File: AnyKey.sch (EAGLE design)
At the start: 101 parts, among them SW1 EVQQ, SW10 EVQQ, SW2 EVQQ, SW3 EVQQ, SW4 EVQQ, SW5 EVQQ, SW6 EVQQ, SW7 EVQQ, SW8 EVQQ, SW9 EVQQ, U3 AP2112K-3.3V

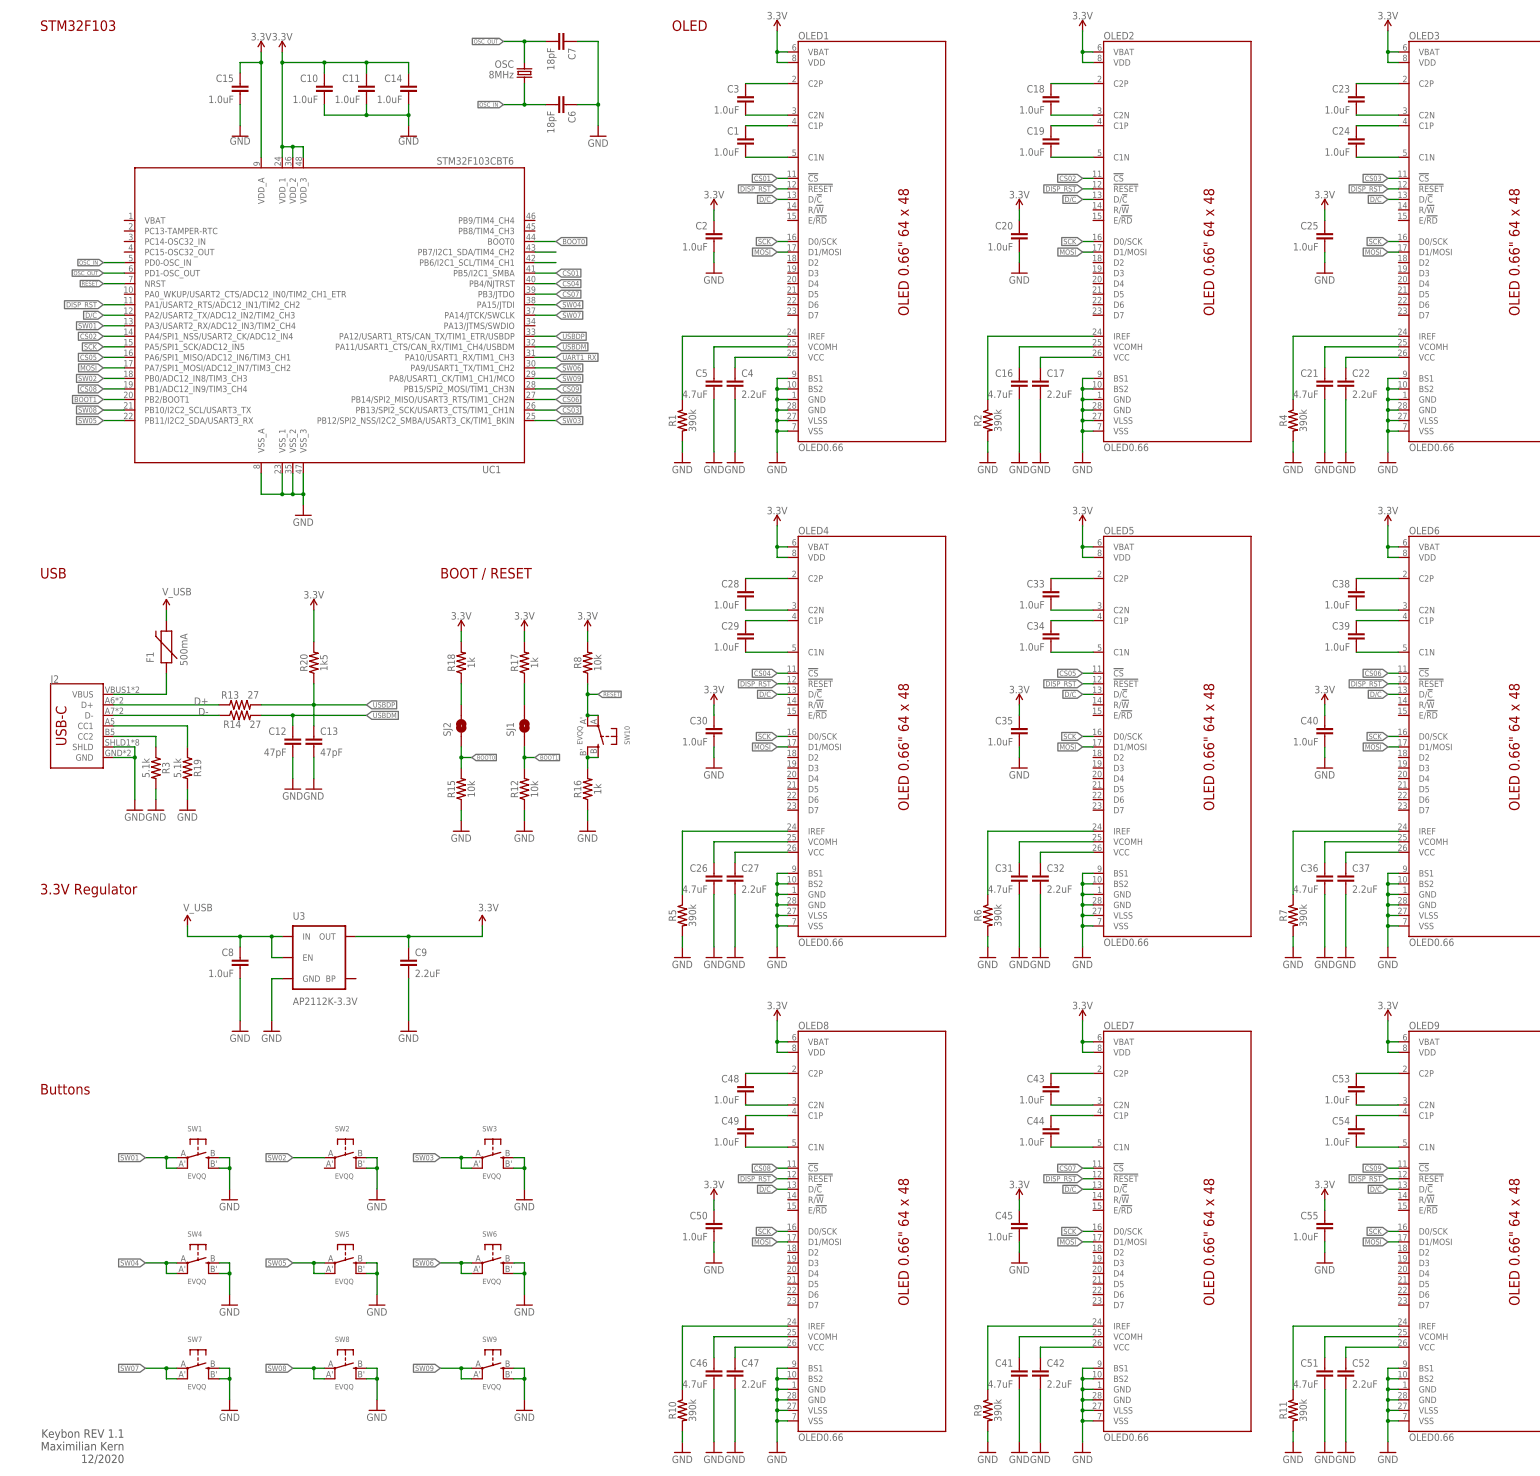
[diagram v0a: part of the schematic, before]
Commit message: Initial cleanup, correctted some misplaced names in top silkscreen
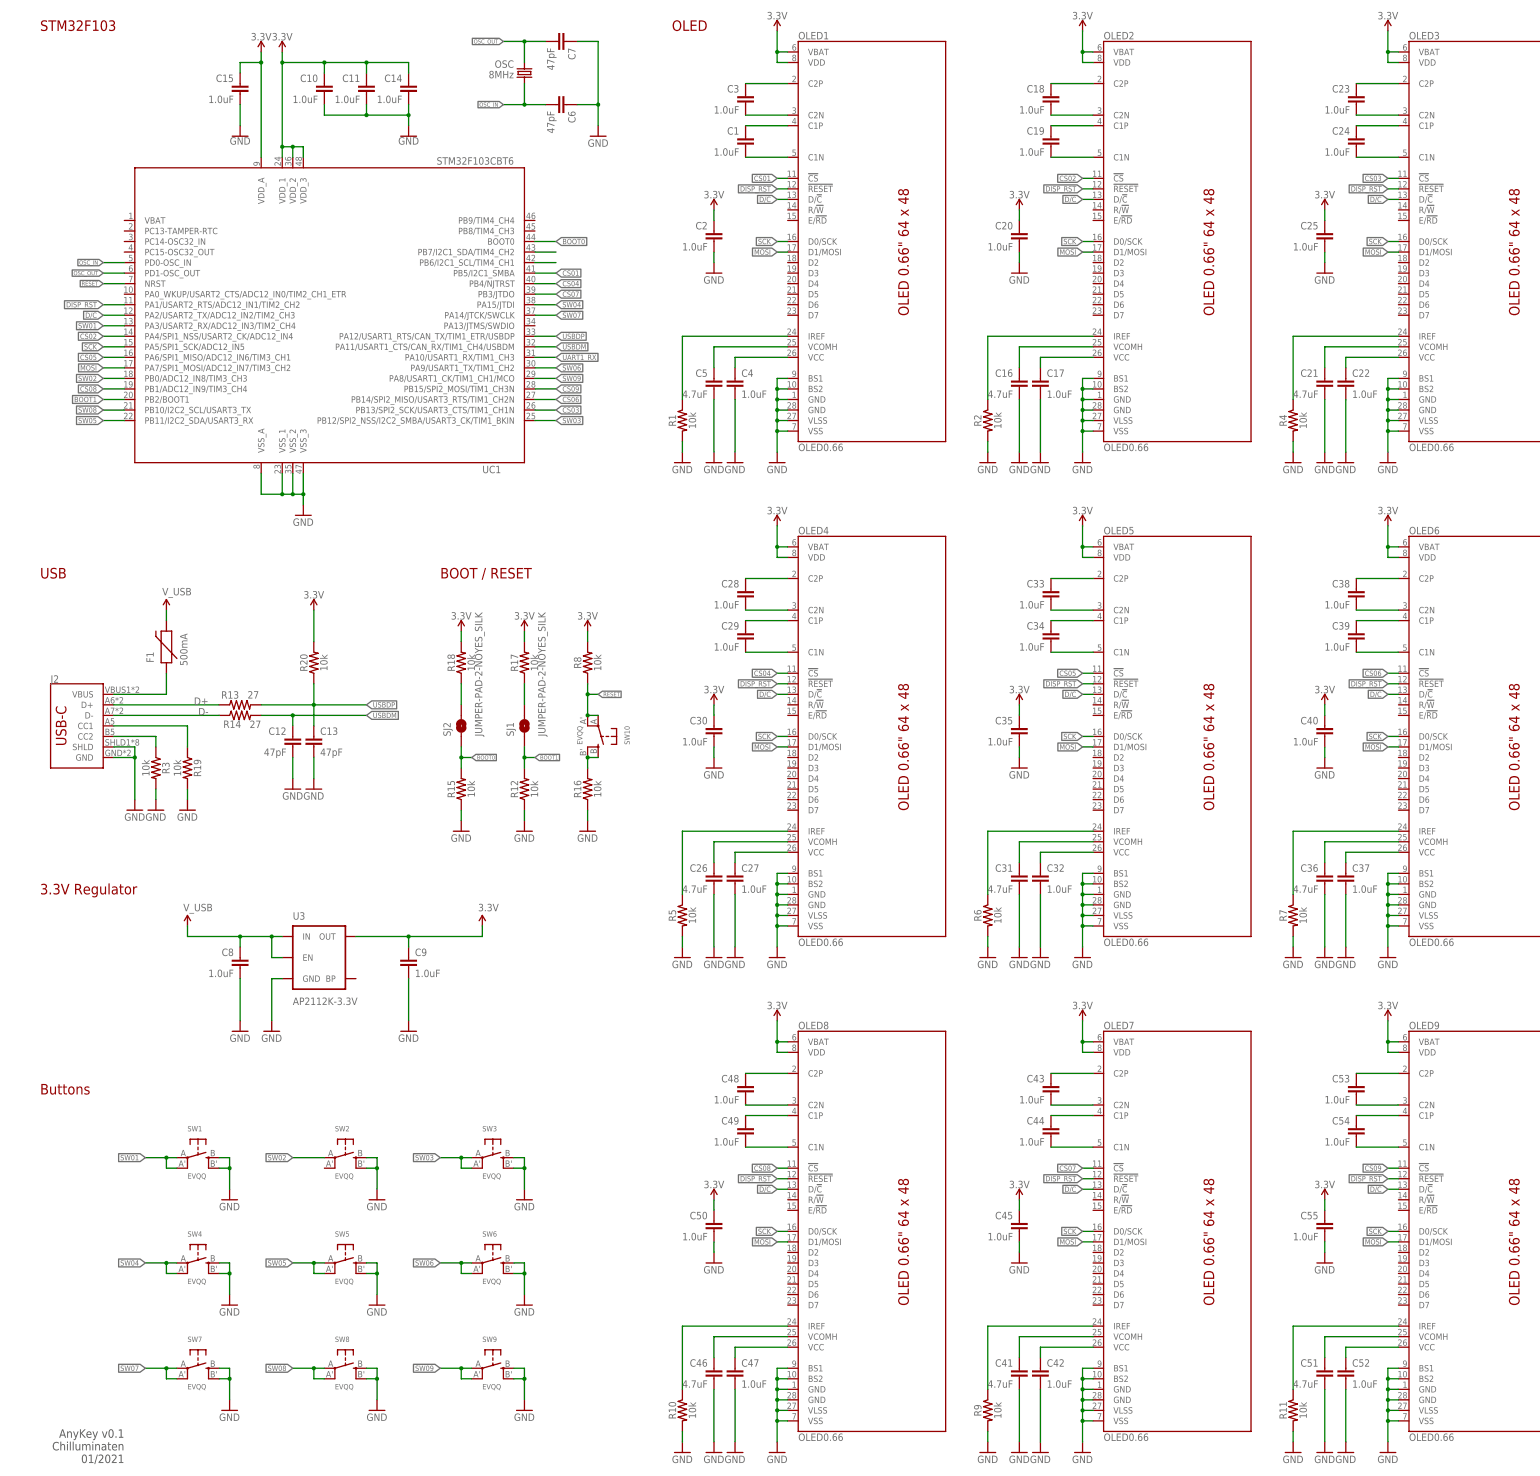
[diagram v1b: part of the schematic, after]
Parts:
- C1, C10, C11, C14, C15, C18, C19, C2, C20, C23, C24, C25, C28, C29, C3, C30, C33, C34, C35, C38, C39, C40, C43, C44, C45, C48, C49, C50, C53, C54, C55, C8: device SparkFun-Capacitors:1.0UF-0805-25V-(+80/-20%) -> AnyKey:1.0UF-0805-25V-(+80/-20%)
- C12, C13: device SparkFun-Capacitors:47PF-0603-50V-5% -> AnyKey:47PF-0603-50V-5%
- C16, C21, C26, C31, C36, C41, C46, C5, C51: device SparkFun-Capacitors:4.7UF0603 -> AnyKey:4.7UF0603
- C17, C22, C27, C32, C37, C4, C42, C47, C52, C9: value 2.2uF -> 1.0uF; device SparkFun-Capacitors:1.0UF-0805-25V-(+80/-20%) -> AnyKey:1.0UF-0805-25V-(+80/-20%)
- C6, C7: value 18pF -> 47pF; device SparkFun-Capacitors:47PF-0603-50V-5% -> AnyKey:47PF-0603-50V-5%
- F1: device SparkFun-PowerIC:PTCSMD -> AnyKey:PTCSMD
- J2: device SparkFun-Connectors:USB_C16PIN -> AnyKey:USB_C16PIN
- OLED1, OLED2, OLED3, OLED4, OLED5, OLED6, OLED7, OLED8, OLED9: device microView-temp:OLED0.66 -> AnyKey:OLED0.66
- OSC: device SparkFun2:CRYSTAL5X3 -> AnyKey:CRYSTAL5X3
- R1, R10, R11, R2, R4, R5, R6, R7, R9: value 390k -> 10k; device SparkFun-Resistors:10KOHM-0603-1/10W-1% -> AnyKey:10KOHM-0603-1/10W-1%
- R12, R15, R8: device SparkFun-Resistors:10KOHM-0603-1/10W-1% -> AnyKey:10KOHM-0603-1/10W-1%
- R13, R14: device SparkFun-Resistors:27OHM1/10W1%(0603)0603-RES -> AnyKey:27OHM1/10W1%(0603)0603-RES
- R16, R17, R18: value 1k -> 10k; device SparkFun-Resistors:10KOHM-0603-1/10W-1% -> AnyKey:10KOHM-0603-1/10W-1%
- R19, R3: value 5.1k -> 10k; device SparkFun-Resistors:10KOHM-0603-1/10W-1% -> AnyKey:10KOHM-0603-1/10W-1%
- R20: value 1k5 -> 10k; device SparkFun-Resistors:10KOHM-0603-1/10W-1% -> AnyKey:10KOHM-0603-1/10W-1%
- SJ1, SJ2: device SparkFun-Passives:JUMPER-PAD-2-NOYES_SILK -> AnyKey:JUMPER-PAD-2-NOYES_SILK
- SW1, SW10, SW2, SW3, SW4, SW5, SW6, SW7, SW8, SW9: device microbuilder:SWITCH_TACT_SMT_EVQQ2_SMALL -> AnyKey:SWITCH_TACT_SMT_EVQQ2_SMALL
- U3: device SparkFun-PowerIC:V_REG_LDOSMD -> AnyKey:V_REG_LDOSMD
- UC1: device stm32:STM32F103CB -> AnyKey:STM32F103CB
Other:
- note added: "AnyKey v0.1 Chilluminaten 01/2021"
- note removed: "Keybon REV 1.1 Maximilian Kern 12/2020"

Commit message: Implemented Auto-Reset, Added WS2812 (WORK IN PROGRESS)
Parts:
- added C56, C57, C58, C59, C60, C61, C62, C63, C64, C65: 1uF, AnyKey:CAPACITOR
- added D1, D10, D2, D3, D4, D5, D6, D7, D8, D9: WS2812_2020, AnyKey:WS2812
- added JP1: DEBUG, AnyKey:PINHD-1X5/90
- added Q1: BC847S, AnyKey:BC847S
- added R21: 1k, AnyKey:RESISTOR
- added R22: 47k, AnyKey:RESISTOR
- added R23: 36k, AnyKey:RESISTOR
- added R24: 10k, AnyKey:RESISTOR
- C1, C10, C11, C14, C15, C18, C19, C2, C20, C23, C24, C25, C28, C29, C3, C30, C33, C34, C35, C38, C39, C40, C43, C44, C45, C48, C49, C50, C53, C54, C55, C8: device AnyKey:1.0UF-0805-25V-(+80/-20%) -> AnyKey:CAPACITOR
- C12, C13: device AnyKey:47PF-0603-50V-5% -> AnyKey:CAPACITOR
- C16, C21, C26, C31, C36, C41, C46, C5, C51: device AnyKey:4.7UF0603 -> AnyKey:CAPACITOR
- C17, C22, C27, C32, C37, C4, C42, C47, C52, C9: value 1.0uF -> 2.2uF; device AnyKey:1.0UF-0805-25V-(+80/-20%) -> AnyKey:CAPACITOR
- C6, C7: value 47pF -> 18pF; device AnyKey:47PF-0603-50V-5% -> AnyKey:CAPACITOR
- J2: value (none) -> SOFNG MC-311D
- R1, R10, R11, R2, R4, R5, R6, R7, R9: value 10k -> 390k; device AnyKey:10KOHM-0603-1/10W-1% -> AnyKey:RESISTOR
- R12, R15, R8: device AnyKey:10KOHM-0603-1/10W-1% -> AnyKey:RESISTOR
- R13, R14: device AnyKey:27OHM1/10W1%(0603)0603-RES -> AnyKey:RESISTOR
- R16, R17, R18: value 10k -> 1k; device AnyKey:10KOHM-0603-1/10W-1% -> AnyKey:RESISTOR
- R19, R3: value 10k -> 5k1; device AnyKey:10KOHM-0603-1/10W-1% -> AnyKey:RESISTOR
- R20: value 10k -> 1k5; device AnyKey:10KOHM-0603-1/10W-1% -> AnyKey:RESISTOR
- SW1, SW10, SW2, SW3, SW4, SW5, SW6, SW7, SW8, SW9: value EVQQ -> B3FS-1000P
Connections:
- removed net SW06: SW6.P, SW6.P1, UC1.PA9/USART1_TX/TIM1_CH2
- removed net SW07: SW7.P, SW7.P1, UC1.PA14/JTCK/SWCLK
- new net DISC: R21.1, UC1.PB9/TIM4_CH4
- new net N$15: Q1.E2, R20.2
- new net N$16: Q1.B2, Q1.C1, R23.2, R24.1
- new net N$17: Q1.B1, R21.2, R22.1
- new net N$18: D1.DO, D2.DI
- new net N$21: D2.DO, D3.DI
- new net N$22: D3.DO, D4.DI
- new net N$23: D4.DO, D5.DI
- new net N$24: D5.DO, D6.DI
- new net N$25: D6.DO, D7.DI
- new net N$26: D7.DO, D8.DI
- new net N$27: D8.DO, D9.DI
- new net N$28: D10.DI, D9.DO
- new net SW06/UART1_TX: JP1.2, SW6.P, SW6.P1, UC1.PA9/USART1_TX/TIM1_CH2
- new net SW07/SWCLK: JP1.4, SW7.P, SW7.P1, UC1.PA14/JTCK/SWCLK
- new net SWDIO: JP1.5, UC1.PA13/JTMS/SWDIO
- new net WS2812: D1.DI, UC1.PB8/TIM4_CH3
- net 3.3V: now also Q1.C2, R22.2; no longer R20.2
- net GND: now also C56.2, C57.2, C58.2, C59.2, C60.2, C61.2, C62.2, C63.2, C64.2, C65.2, D1.GND, D10.GND, D2.GND, D3.GND, D4.GND, D5.GND, D6.GND, D7.GND, D8.GND, D9.GND, JP1.3, Q1.E1, R23.1
- net SW02: now also SW2.P1
- net UART1_RX: now also JP1.1
- net V_USB: now also C56.1, C57.1, C58.1, C59.1, C60.1, C61.1, C62.1, C63.1, C64.1, C65.1, D1.VCC, D10.VCC, D2.VCC, D3.VCC, D4.VCC, D5.VCC, D6.VCC, D7.VCC, D8.VCC, D9.VCC, R24.2
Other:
- note added: "Lightning"
- moved on the sheet: C12, C13, F1, J2, R13, R14, R19, R20, R3
